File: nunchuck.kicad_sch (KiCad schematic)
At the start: 56 parts, among them J2 USB_C_Receptacle_USB2.0_14P, J3 USB_C_Receptacle_USB2.0_14P, SW1 BOOT, SW2 RESET, SW3 BOOT, SW4 RESET, U1 CH552T, U2 CH552T, U3 USBLC6-2SC6, U4 USBLC6-2SC6

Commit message: before hexing
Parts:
- added C10, C11, C12, C9: 1uF, Capacitor_SMD:C_0603_1608Metric_Pad1.08x0.95mm_HandSolder, symbol Device:C
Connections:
- net GND: now also C10.2, C11.2, C12.2, C9.2
- net at J2.S1 (SHIELD): now also C10.1, C11.1, C12.1, C9.1
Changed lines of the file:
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@@
   (junction (at 53.34 44.45) (diameter 0) (color 0 0 0 0)
   )
+  (junction (at 233.045 152.4) (diameter 0) (color 0 0 0 0)
+  )
   (junction (at 99.06 26.67) (diameter 0) (color 0 0 0 0)
   )
@@
   (junction (at 53.34 31.75) (diameter 0) (color 0 0 0 0)
   )
+  (junction (at 233.045 160.02) (diameter 0) (color 0 0 0 0)
+  )
   (junction (at 137.16 67.31) (diameter 0) (color 0 0 0 0)
   )
@@
   (junction (at 143.51 74.93) (diameter 0) (color 0 0 0 0)
   )
+  (junction (at 226.695 152.4) (diameter 0) (color 0 0 0 0)
+  )
   (junction (at 88.9 31.75) (diameter 0) (color 0 0 0 0)
   )
+  (junction (at 220.345 152.4) (diameter 0) (color 0 0 0 0)
+  )
+  (junction (at 220.345 160.02) (diameter 0) (color 0 0 0 0)
+  )
   (junction (at 149.86 67.31) (diameter 0) (color 0 0 0 0)
   )
@@
   )
   (junction (at 172.72 36.83) (diameter 0) (color 0 0 0 0)
+  )
+  (junction (at 226.695 160.02) (diameter 0) (color 0 0 0 0)
   )
   (junction (at 76.2 29.21) (diameter 0) (color 0 0 0 0)
@@
     (stroke (width 0) (type default))
   )
+  (wire (pts (xy 213.995 160.02) (xy 220.345 160.02))
+    (stroke (width 0) (type default))
+  )
   (wire (pts (xy 255.905 125.73) (xy 266.065 125.73))
     (stroke (width 0) (type default))
@@
     (stroke (width 0) (type default))
   )
+  (wire (pts (xy 220.345 160.02) (xy 226.695 160.02))
+    (stroke (width 0) (type default))
+  )
   (wire (pts (xy 91.44 148.59) (xy 99.06 148.59))
     (stroke (width 0) (type default))
@@
     (stroke (width 0) (type default))
   )
+  (wire (pts (xy 220.345 152.4) (xy 226.695 152.4))
+    (stroke (width 0) (type default))
+  )
   (wire (pts (xy 172.72 41.91) (xy 172.72 44.45))
     (stroke (width 0) (type default))
@@
     (stroke (width 0) (type default))
   )
+  (wire (pts (xy 226.695 160.02) (xy 233.045 160.02))
+    (stroke (width 0) (type default))
+  )
   (wire (pts (xy 143.51 74.93) (xy 149.86 74.93))
     (stroke (width 0) (type default))
@@
     (stroke (width 0) (type default))
   )
+  (wire (pts (xy 226.695 152.4) (xy 233.045 152.4))
+    (stroke (width 0) (type default))
+  )
   (wire (pts (xy 111.76 41.91) (xy 119.38 41.91))
     (stroke (width 0) (type default))
@@
     (stroke (width 0) (type default))
   )
+  (wire (pts (xy 213.995 152.4) (xy 220.345 152.4))
+    (stroke (width 0) (type default))
+  )
   (wire (pts (xy 130.81 74.93) (xy 137.16 74.93))
     (stroke (width 0) (type default))
@@
     (property "Intersheetrefs" "${INTERSHEET_REFS}" (at 204.2667 35.56 0)
       (effects (font (size 1.27 1.27)) (justify right) hide)
+    )
+  )
+  (symbol (lib_id "Device:C") (at 233.045 156.21 0) (unit 1)
+    (in_bom yes) (on_board yes) (dnp no) (fields_autoplaced)
+    (property "Reference" "C12" (at 236.855 154.94 0)
+      (effects (font (size 1.27 1.27)) (justify left))
+    )
+    (property "Value" "1uF" (at 236.855 157.48 0)
+      (effects (font (size 1.27 1.27)) (justify left))
+    )
+    (property "Footprint" "Capacitor_SMD:C_0603_1608Metric_Pad1.08x0.95mm_HandSolder" (at 234.0102 160.02 0)
+      (effects (font (size 1.27 1.27)) hide)
+    )
+    (property "Datasheet" "~" (at 233.045 156.21 0)
+      (effects (font (size 1.27 1.27)) hide)
+    )
+    (pin "2")
+    (pin "1")
+    (instances
+      (project "nunchuck"
+        (path "/b46ad75c-c7a1-4bfe-a2f6-0c79981e5dbf"
+          (reference "C12") (unit 1)
+        )
+      )
+    )
+  )
+  (symbol (lib_id "power:GND") (at 233.045 160.02 0) (mirror y) (unit 1)
+    (in_bom yes) (on_board yes) (dnp no)
+    (property "Reference" "#PWR030" (at 233.045 166.37 0)
+      (effects (font (size 1.27 1.27)) hide)
+    )
+    (property "Value" "GND" (at 233.045 165.1 0)
+      (effects (font (size 1.27 1.27)))
+    )
+    (property "Footprint" "" (at 233.045 160.02 0)
+      (effects (font (size 1.27 1.27)) hide)
+    )
+    (property "Datasheet" "" (at 233.045 160.02 0)
+      (effects (font (size 1.27 1.27)) hide)
+    )
+    (pin "1")
+    (instances
+      (project "nunchuck"
+        (path "/b46ad75c-c7a1-4bfe-a2f6-0c79981e5dbf"
+          (reference "#PWR030") (unit 1)
+        )
+      )
     )
   )
@@
     )
   )
+  (symbol (lib_id "Device:C") (at 220.345 156.21 0) (unit 1)
+    (in_bom yes) (on_board yes) (dnp no) (fields_autoplaced)
+    (property "Reference" "C10" (at 224.155 154.94 0)
+      (effects (font (size 1.27 1.27)) (justify left))
+    )
+    (property "Value" "1uF" (at 224.155 157.48 0)
+      (effects (font (size 1.27 1.27)) (justify left))
+    )
+    (property "Footprint" "Capacitor_SMD:C_0603_1608Metric_Pad1.08x0.95mm_HandSolder" (at 221.3102 160.02 0)
+      (effects (font (size 1.27 1.27)) hide)
+    )
+    (property "Datasheet" "~" (at 220.345 156.21 0)
+      (effects (font (size 1.27 1.27)) hide)
+    )
+    (pin "2")
+    (pin "1")
+    (instances
+      (project "nunchuck"
+        (path "/b46ad75c-c7a1-4bfe-a2f6-0c79981e5dbf"
+          (reference "C10") (unit 1)
+        )
+      )
+    )
+  )
   (symbol (lib_id "Diode:BAV70") (at 76.2 21.59 0) (mirror y) (unit 1)
     (in_bom yes) (on_board yes) (dnp no)
@@
         (path "/b46ad75c-c7a1-4bfe-a2f6-0c79981e5dbf"
           (reference "#PWR016") (unit 1)
+        )
+      )
+    )
+  )
+  (symbol (lib_id "Device:C") (at 226.695 156.21 0) (unit 1)
+    (in_bom yes) (on_board yes) (dnp no) (fields_autoplaced)
+    (property "Reference" "C11" (at 230.505 154.94 0)
+      (effects (font (size 1.27 1.27)) (justify left))
+    )
+    (property "Value" "1uF" (at 230.505 157.48 0)
+      (effects (font (size 1.27 1.27)) (justify left))
+    )
+    (property "Footprint" "Capacitor_SMD:C_0603_1608Metric_Pad1.08x0.95mm_HandSolder" (at 227.6602 160.02 0)
+      (effects (font (size 1.27 1.27)) hide)
+    )
+    (property "Datasheet" "~" (at 226.695 156.21 0)
+      (effects (font (size 1.27 1.27)) hide)
+    )
+    (pin "2")
+    (pin "1")
+    (instances
+      (project "nunchuck"
+        (path "/b46ad75c-c7a1-4bfe-a2f6-0c79981e5dbf"
+          (reference "C11") (unit 1)
         )
       )
@@
         )
       )
+    )
+  )
+  (symbol (lib_id "Device:C") (at 213.995 156.21 0) (unit 1)
+    (in_bom yes) (on_board yes) (dnp no) (fields_autoplaced)
+    (property "Reference" "C9" (at 217.805 154.94 0)
+      (effects (font (size 1.27 1.27)) (justify left))
+    )
+    (property "Value" "1uF" (at 217.805 157.48 0)
+      (effects (font (size 1.27 1.27)) (justify left))
+    )
+    (property "Footprint" "Capacitor_SMD:C_0603_1608Metric_Pad1.08x0.95mm_HandSolder" (at 214.9602 160.02 0)
+      (effects (font (size 1.27 1.27)) hide)
+    )
+    (property "Datasheet" "~" (at 213.995 156.21 0)
+      (effects (font (size 1.27 1.27)) hide)
+    )
+    (pin "2")
+    (pin "1")
+    (instances
+      (project "nunchuck"
+        (path "/b46ad75c-c7a1-4bfe-a2f6-0c79981e5dbf"
+          (reference "C9") (unit 1)
+        )
+      )

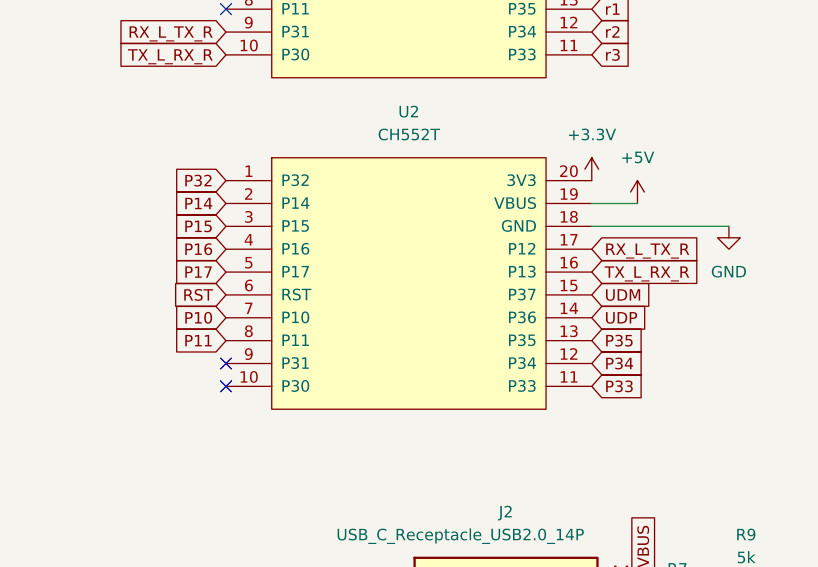
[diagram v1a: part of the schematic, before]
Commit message: added missing connections on back side
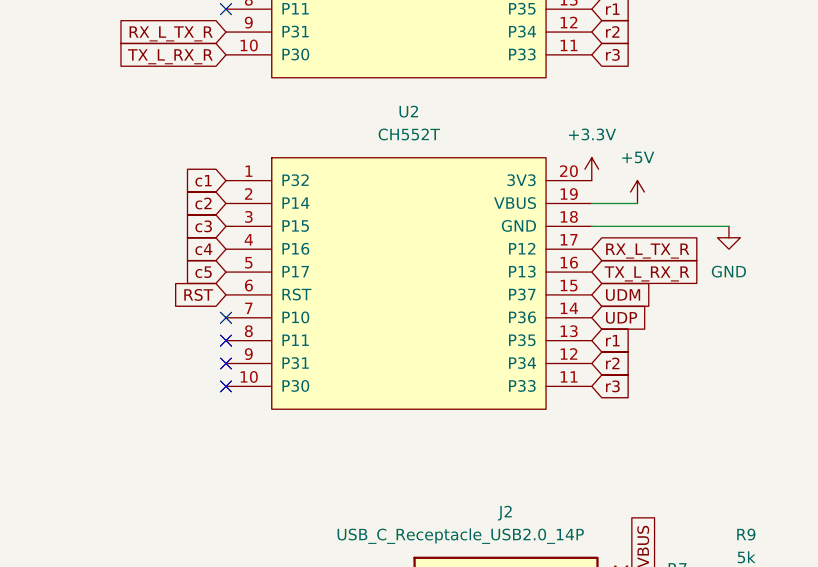
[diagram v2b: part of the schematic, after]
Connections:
- net P14 is gone; now on net c2: U2.2 (P14)
- net P15 is gone; now on net c3: U2.3 (P15)
- net P16 is gone; now on net c4: U2.4 (P16)
- net P17 is gone; now on net c5: U2.5 (P17)
- net P32 is gone; now on net c1: U2.1 (P32)
- net P33 is gone; now on net r3: U2.11 (P33)
- net P34 is gone; now on net r2: U2.12 (P34)
- net P35 is gone; now on net r1: U2.13 (P35)
- net P10: no longer names the net of U2.7 (P10)
- net P11: no longer names the net of U2.8 (P11)
- no-connect marks 9 -> 11

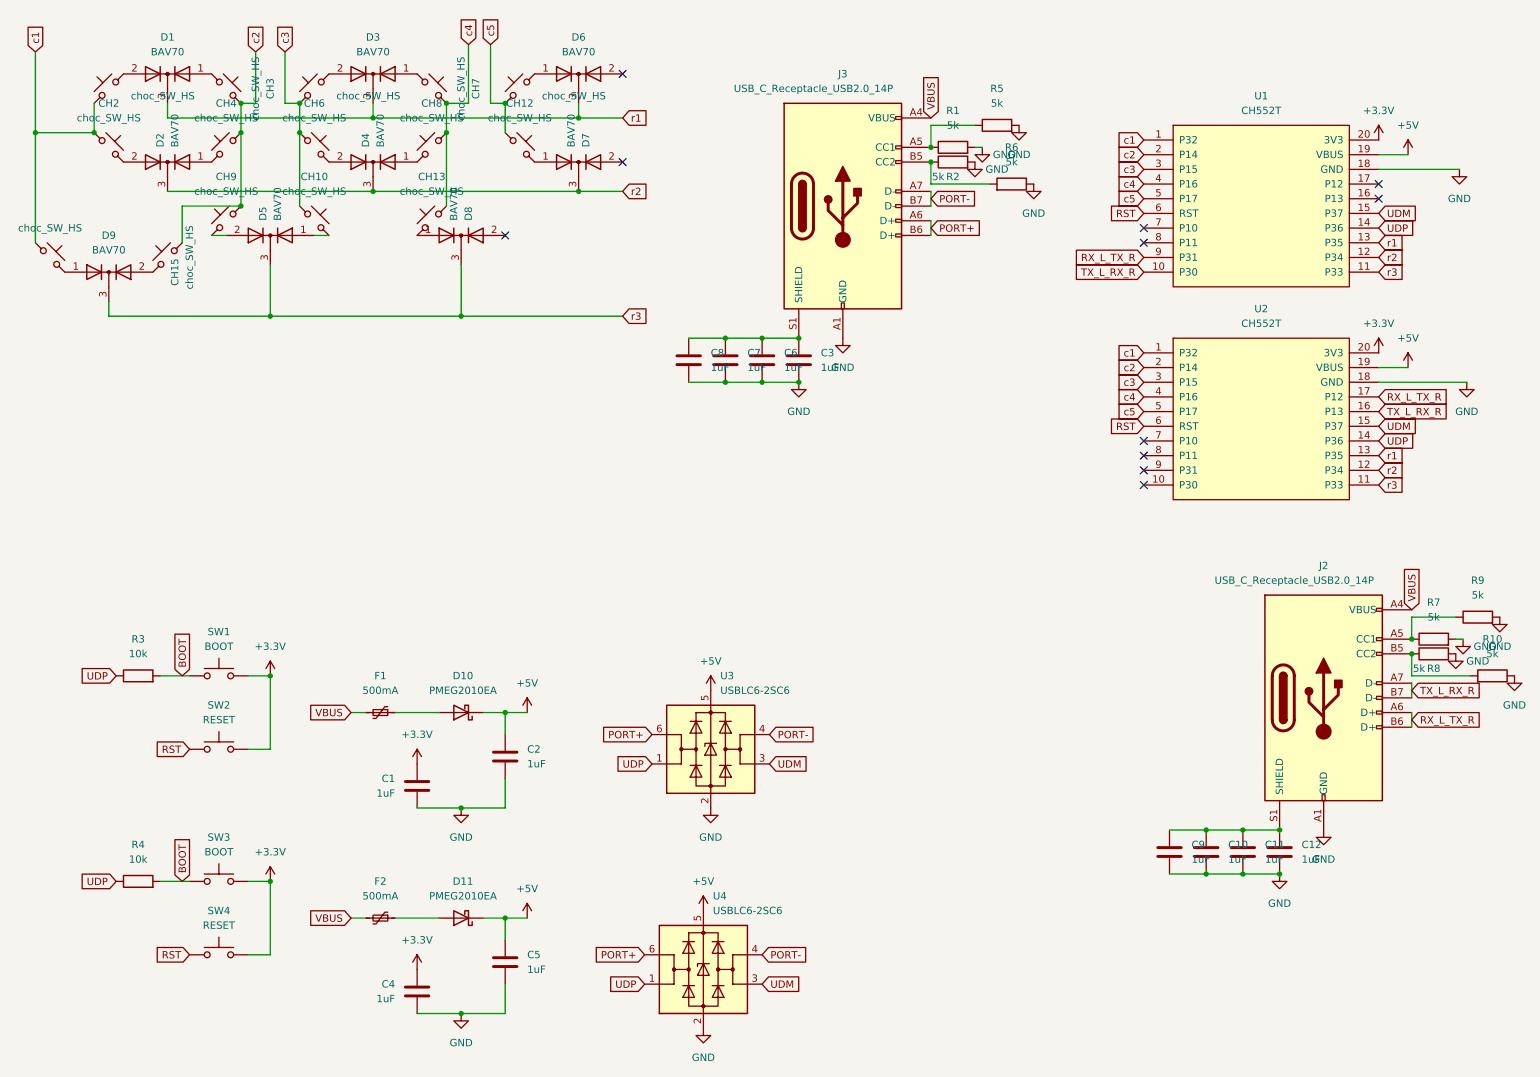
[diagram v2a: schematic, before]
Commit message: corrected wrongly connected thumb key, and removed unnecessary 5k resistors
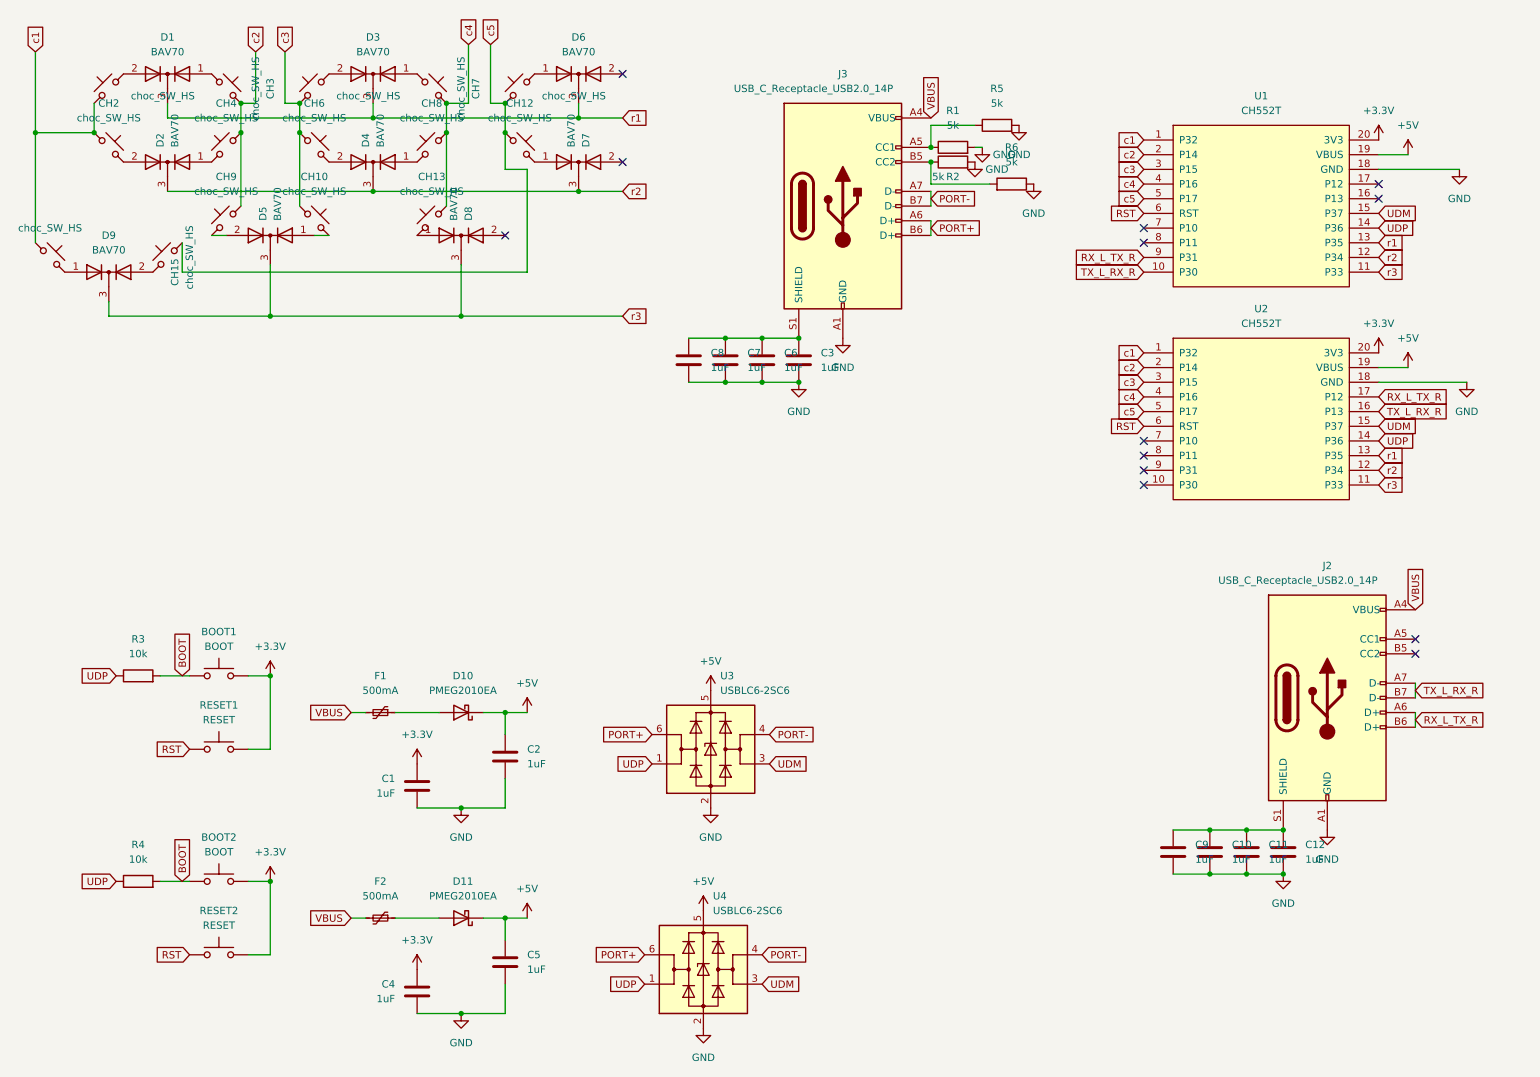
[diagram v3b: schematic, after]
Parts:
- removed R10, R7, R8, R9: 5k, Resistor_SMD:R_0603_1608Metric_Pad0.98x0.95mm_HandSolder, symbol Device:R
- renumbered SW1 to BOOT1, SW3 to BOOT2, SW2 to RESET1, SW4 to RESET2
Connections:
- net c2: no longer CH15.1
- net c5: now also CH15.1
- no-connect marks 11 -> 13
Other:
- moved on the sheet: C10, C11, C12, C9, J2
